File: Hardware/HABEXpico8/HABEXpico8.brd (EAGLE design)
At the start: 160 x 100 mm, 28 parts, among them Q1 2.5A/30V, U1 LTC3106, U2 EVA-8M, U3 STM32L011G4, Y1 ABS07-120-32.768KHZ-T

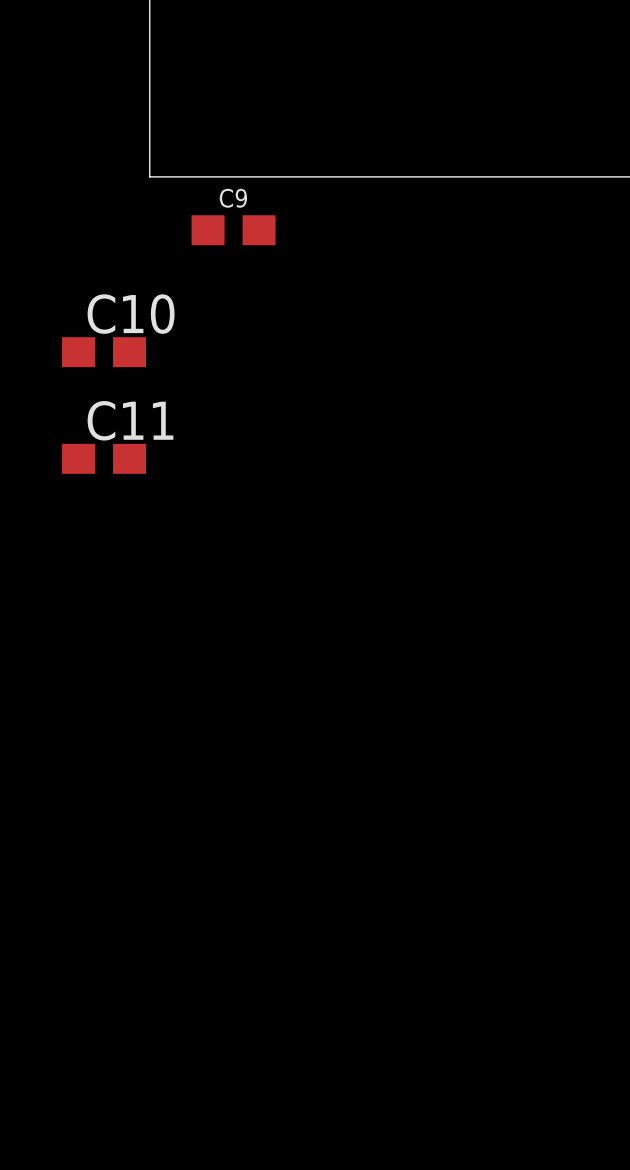
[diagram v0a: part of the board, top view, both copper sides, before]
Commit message: Updated schematic design
Power save support ICs, updated power budget
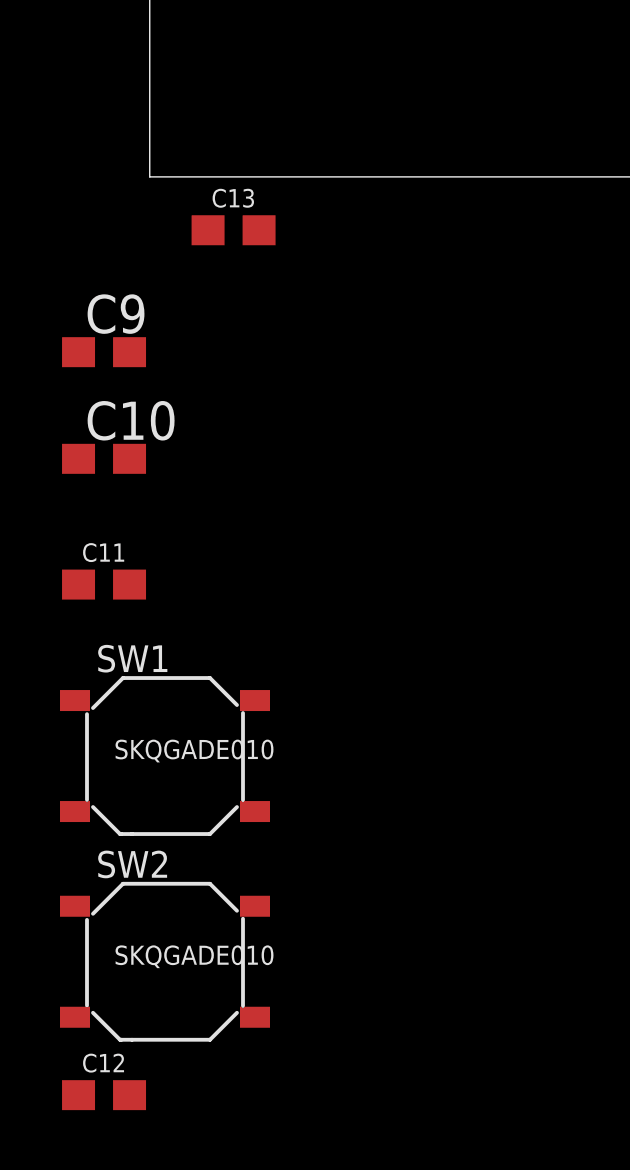
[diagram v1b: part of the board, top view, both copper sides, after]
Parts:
- added C12, C13: 0.1uF, SparkFun-Capacitors:0603
- added SW1, SW2: SKQGADE010, Seeed-Switch:SW4-SMD-5.2X5.2X1.5MM
- C11: value 6pF -> 0.1uF; device rcl:C0603 -> SparkFun-Capacitors:0603
- C9: value 0.1uF -> 6pF; device SparkFun-Capacitors:0603 -> rcl:C0603
- moved C9 5.93 mm to (-1.52, -5.84)
- moved C11 4.19 mm to (-1.52, -13.6)
- moved C10 3.56 mm to (-1.52, -9.40)
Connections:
- new net MCU_BOOT0: C12.1, SW2.2, U3.1
- new net N$8: U3.3
- new net N$9: U3.2
- new net SWCLK: U3.22
- new net SWDIO: U3.21
- net 3.3V: now also C13.1; no longer C9.1
- net GND: now also C12.2, C13.2, SW1.4, SW2.4
- net MCU_RESET: now also C11.1, SW1.2
- net N$6: now also C9.1; no longer C10.1
- net N$7: now also C10.1; no longer C11.1
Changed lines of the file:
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@@
 <attribute name="PROD_ID" value="RES-07863" x="18.796" y="34.163" size="1.778" layer="27" display="off"/>
 </element>
-<element name="C9" library="SparkFun-Capacitors" library_urn="urn:adsk.eagle:library:510" package="0603" package3d_urn="urn:adsk.eagle:package:37414/1" value="0.1uF" x="2.794" y="-1.778">
+<element name="C13" library="SparkFun-Capacitors" library_urn="urn:adsk.eagle:library:510" package="0603" package3d_urn="urn:adsk.eagle:package:37414/1" value="0.1uF" x="2.794" y="-1.778">
 <attribute name="PROD_ID" value="CAP-08604" x="2.794" y="-1.778" size="1.778" layer="27" display="off"/>
 </element>
@@
 <attribute name="PROD_ID" value="XTAL-13062" x="27.051" y="26.924" size="1.778" layer="27" rot="R90" display="off"/>
 </element>
-<element name="C10" library="rcl" library_urn="urn:adsk.eagle:library:334" package="C0603" package3d_urn="urn:adsk.eagle:package:23616/2" value="6pF" x="-1.524" y="-5.842"/>
-<element name="C11" library="rcl" library_urn="urn:adsk.eagle:library:334" package="C0603" package3d_urn="urn:adsk.eagle:package:23616/2" value="6pF" x="-1.524" y="-9.398"/>
+<element name="C9" library="rcl" library_urn="urn:adsk.eagle:library:334" package="C0603" package3d_urn="urn:adsk.eagle:package:23616/2" value="6pF" x="-1.524" y="-5.842"/>
+<element name="C10" library="rcl" library_urn="urn:adsk.eagle:library:334" package="C0603" package3d_urn="urn:adsk.eagle:package:23616/2" value="6pF" x="-1.524" y="-9.398"/>
+<element name="C11" library="SparkFun-Capacitors" library_urn="urn:adsk.eagle:library:510" package="0603" package3d_urn="urn:adsk.eagle:package:37414/1" value="0.1uF" x="-1.524" y="-13.589">
+<attribute name="PROD_ID" value="CAP-08604" x="-1.524" y="-13.589" size="1.778" layer="27" display="off"/>
+</element>
+<element name="SW1" library="Seeed-Switch" library_urn="urn:adsk.eagle:library:476" package="SW4-SMD-5.2X5.2X1.5MM" package3d_urn="urn:adsk.eagle:package:32992/1" value="SKQGADE010" x="0.508" y="-19.304">
+<attribute name="MPN" value="SKQGADE010" x="0.508" y="-19.304" size="1.778" layer="27" display="off"/>
+</element>
+<element name="C12" library="SparkFun-Capacitors" library_urn="urn:adsk.eagle:library:510" package="0603" package3d_urn="urn:adsk.eagle:package:37414/1" value="0.1uF" x="-1.524" y="-30.607">
+<attribute name="PROD_ID" value="CAP-08604" x="-1.524" y="-23.749" size="1.778" layer="27" display="off"/>
+</element>
+<element name="SW2" library="Seeed-Switch" library_urn="urn:adsk.eagle:library:476" package="SW4-SMD-5.2X5.2X1.5MM" package3d_urn="urn:adsk.eagle:package:32992/1" value="SKQGADE010" x="0.508" y="-26.162">
+<attribute name="MPN" value="SKQGADE010" x="0.508" y="-29.464" size="1.778" layer="27" display="off"/>
+</element>
 </elements>
 <signals>
@@
 <contactref element="C8" pad="2"/>
 <contactref element="U3" pad="16"/>
+<contactref element="C13" pad="2"/>
 <contactref element="C9" pad="2"/>
 <contactref element="C10" pad="2"/>
 <contactref element="C11" pad="2"/>
+<contactref element="SW1" pad="4"/>
+<contactref element="C12" pad="2"/>
+<contactref element="SW2" pad="4"/>
 <wire x1="67.183" y1="29.591" x2="61.742" y2="38.624" width="0" layer="19" extent="1-1"/>
 <wire x1="69.303" y1="25.527" x2="67.183" y2="29.591" width="0" layer="19" extent="1-1"/>
@@
 <wire x1="-0.674" y1="-5.842" x2="3.644" y2="-1.778" width="0" layer="19" extent="1-1"/>
 <wire x1="-0.674" y1="-9.398" x2="-0.674" y2="-5.842" width="0" layer="19" extent="1-1"/>
+<wire x1="-0.674" y1="-13.589" x2="-0.674" y2="-9.398" width="0" layer="19" extent="1-1"/>
+<wire x1="3.508" y1="-21.154" x2="-0.674" y2="-13.589" width="0" layer="19" extent="1-1"/>
+<wire x1="3.508" y1="-28.012" x2="3.508" y2="-21.154" width="0" layer="19" extent="1-1"/>
+<wire x1="-0.674" y1="-30.607" x2="3.508" y2="-28.012" width="0" layer="19" extent="1-1"/>
 </signal>
 <signal name="2">
@@
 <contactref element="U3" pad="17"/>
 <contactref element="U3" pad="5"/>
-<contactref element="C9" pad="1"/>
+<contactref element="C13" pad="1"/>
 <wire x1="57.892" y1="39.124" x2="61.742" y2="39.124" width="0" layer="19" extent="1-1"/>
 <wire x1="42.303" y1="26.921" x2="57.892" y2="39.124" width="0" layer="19" extent="1-1"/>
@@
 <signal name="MCU_RESET">
 <contactref element="U3" pad="4"/>
+<contactref element="SW1" pad="2"/>
+<contactref element="C11" pad="1"/>
+<wire x1="3.508" y1="-17.454" x2="57.892" y2="39.624" width="0" layer="19" extent="1-1"/>
+<wire x1="-2.374" y1="-13.589" x2="3.508" y2="-17.454" width="0" layer="19" extent="1-1"/>
 </signal>
 <signal name="N$6">
 <contactref element="U2" pad="9"/>
 <contactref element="Y1" pad="P$1"/>
-<contactref element="C10" pad="1"/>
+<contactref element="C9" pad="1"/>
 <wire x1="27.051" y1="25.674" x2="30.378" y2="26.483" width="0" layer="19" extent="1-1"/>
 <wire x1="-2.374" y1="-5.842" x2="27.051" y2="25.674" width="0" layer="19" extent="1-1"/>
@@
 <contactref element="U2" pad="8"/>
 <contactref element="Y1" pad="P$2"/>
-<contactref element="C11" pad="1"/>
+<contactref element="C10" pad="1"/>
 <wire x1="27.051" y1="28.174" x2="30.378" y2="27.133" width="0" layer="19" extent="1-1"/>
 <wire x1="-2.374" y1="-9.398" x2="27.051" y2="28.174" width="0" layer="19" extent="1-1"/>
 </signal>
+<signal name="MCU_BOOT0">
+<contactref element="U3" pad="1"/>
+<contactref element="SW2" pad="2"/>
+<contactref element="C12" pad="1"/>
+<wire x1="3.508" y1="-24.312" x2="57.792" y2="41.124" width="0" layer="19" extent="1-1"/>
+<wire x1="-2.374" y1="-30.607" x2="3.508" y2="-24.312" width="0" layer="19" extent="1-1"/>
+</signal>
+<signal name="N$8">
+<contactref element="U3" pad="3"/>
+</signal>
+<signal name="N$9">
+<contactref element="U3" pad="2"/>
+</signal>
+<signal name="SWDIO">
+<contactref element="U3" pad="21"/>
+</signal>
+<signal name="SWCLK">
+<contactref element="U3" pad="22"/>
+</signal>
 </signals>
